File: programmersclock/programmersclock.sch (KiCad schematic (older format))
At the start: 18 parts, among them IC1 MCP2200, J3 USB_OTG, SW1 RST, U1 MCP7940N, U2 LM1117-3.3, U3 ESP-12E, Y1 32.768 kHz, Y2 12 MHz

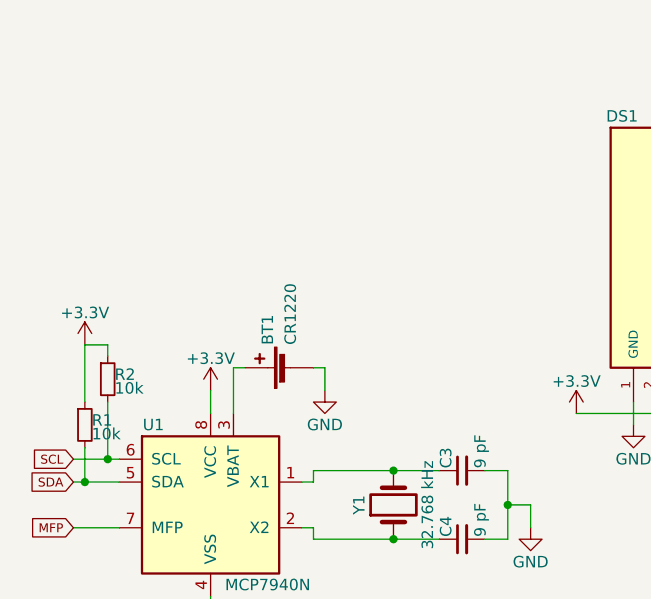
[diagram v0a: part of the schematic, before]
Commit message: Added recommended battery circuity for the MCP7940N
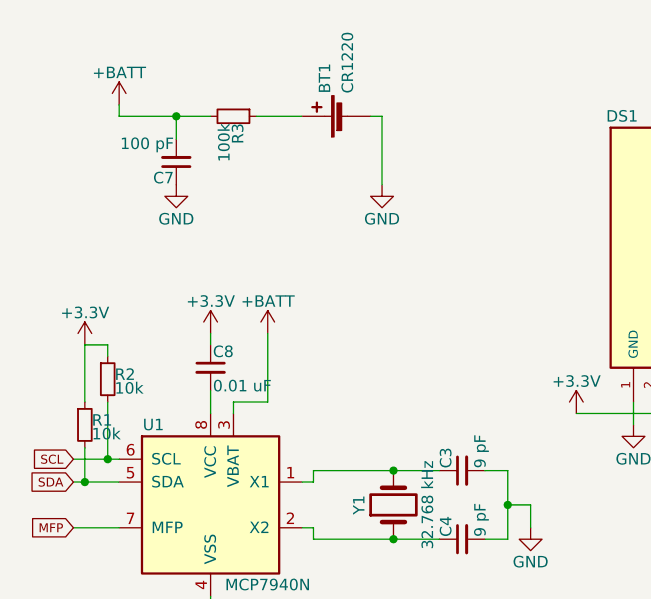
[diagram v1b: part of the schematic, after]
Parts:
- added C7: 100 pF, Capacitors_SMD:C_0805, symbol C_Small
- added C8: 0.01 uF, Capacitors_SMD:C_0805, symbol C_Small
- added R3: 100k, Resistors_SMD:R_0805, symbol R_Small
- C1, C2: footprint Capacitors_SMD:C_1206_HandSoldering -> Capacitors_SMD:C_1206
- C3, C4, C5, C6: footprint Capacitors_SMD:C_0805_HandSoldering -> Capacitors_SMD:C_0805
- R1, R2: footprint Resistors_SMD:R_0805_HandSoldering -> Resistors_SMD:R_0805
- Y2: footprint Crystals:Crystal_SMD_3225-4pin_3.2x2.5mm -> Crystals:Crystal_SMD_5032-2pin_5.0x3.2mm
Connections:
- net +3V3: now also C8.1; no longer U1.8 (VCC)
- net GND: now also C7.1
- net at BT1.1 (+): now also R3.1; no longer U1.3 (VBAT)
- new net: C8.2, U1.8 (VCC)
- new net +BATT: C7.2, R3.2, U1.3 (VBAT)
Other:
- moved on the sheet: BT1

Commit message: Replaced battery with CR2032 and general layout rework
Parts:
- BT1: value CR1220 -> CR2032; footprint Battery_Holders_extra:BatteryHolder_CoinCell_Keystone_3000 -> Battery_Holders_Clone:Keystone_3034_1x20mm-CoinCell
- U2: symbol LM1117-3.3 -> LM1117-3.3-RESCUE-programmersclock
- Y2: footprint Crystals:Crystal_SMD_5032-2pin_5.0x3.2mm -> Crystals:Crystal_SMD_Abracon_ABM3-2pin_5.0x3.2mm
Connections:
- net at U3.10 (GPIO15): no longer DS1.6 (E)
- net at U3.13 (GPIO4): no longer DS1.5 (R/W)
- net at U3.14 (GPIO5): no longer DS1.4 (RS)
- net at U3.5 (GPIO14): now also DS1.6 (E)
- net at U3.6 (GPIO12): now also DS1.5 (R/W)
- net at U3.7 (GPIO13): now also DS1.4 (RS)
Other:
- moved on the sheet: SW1, U3
